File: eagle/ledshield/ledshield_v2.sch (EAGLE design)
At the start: 15 parts, among them U3 PCA9685

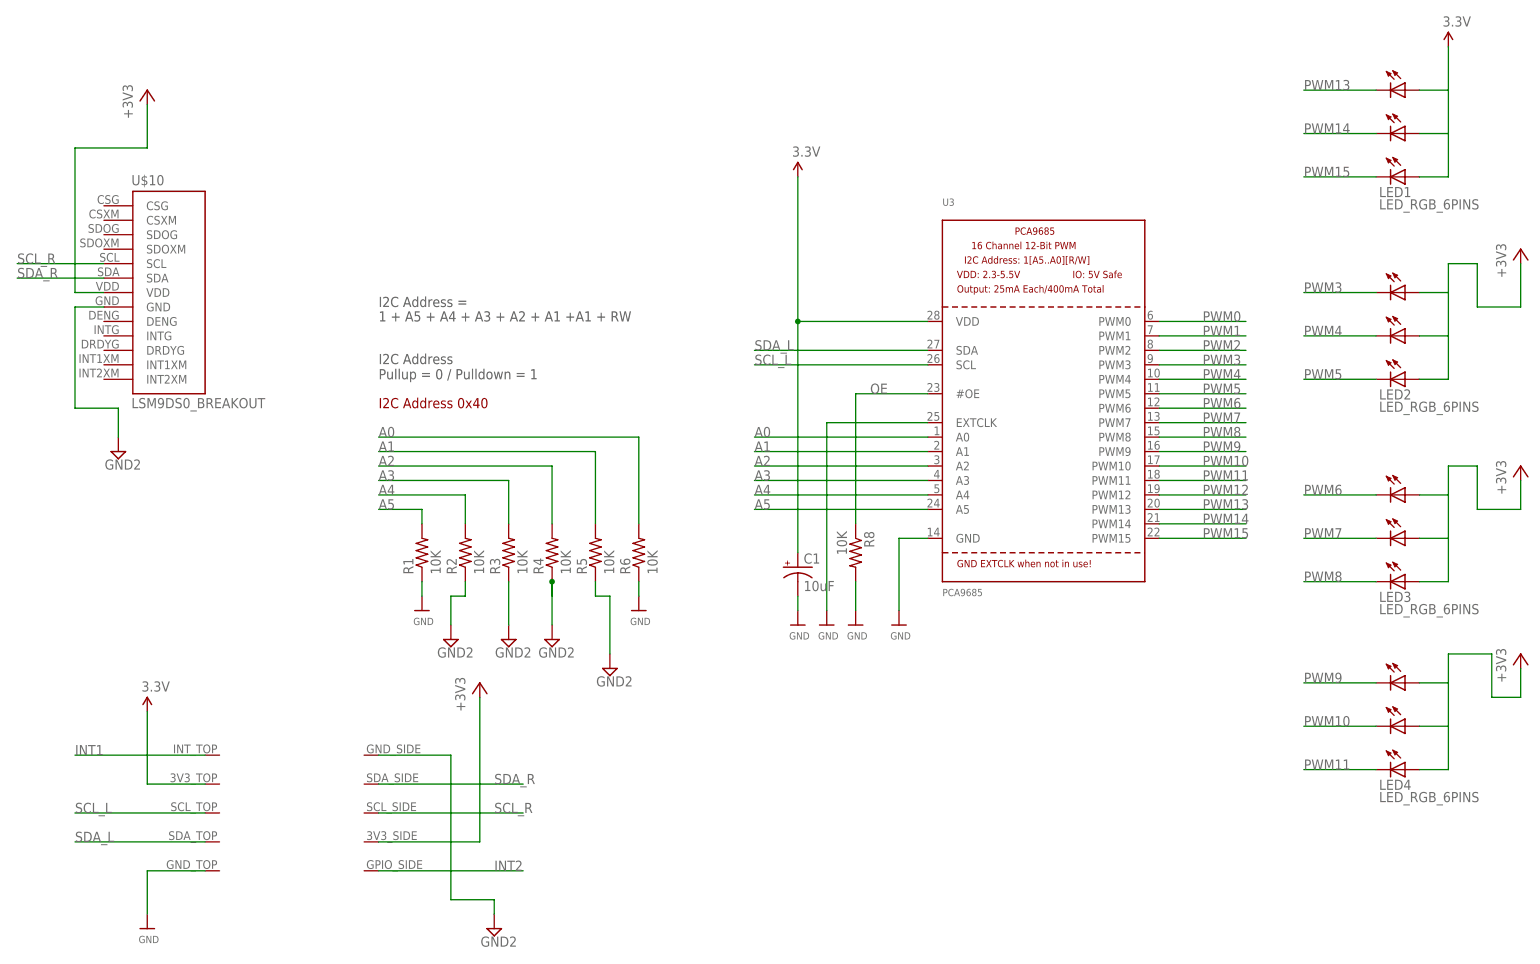
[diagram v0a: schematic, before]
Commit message: updated led shield design with common ground and passing design and electrical checks also started bluetooth/arduino communication to work in reverse from processing to arduino
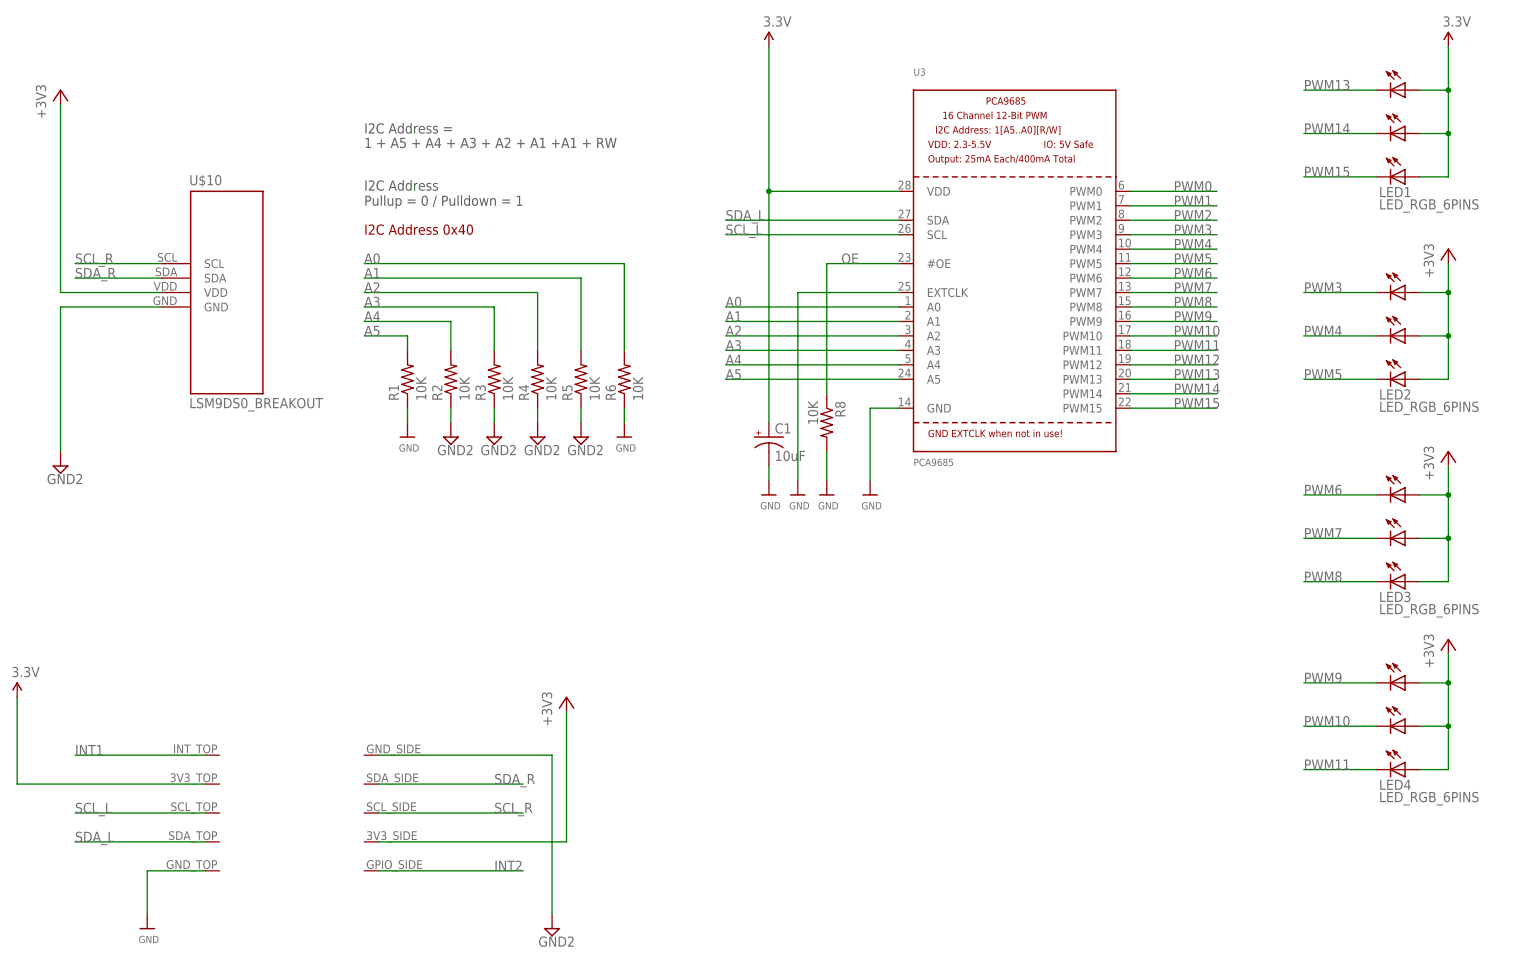
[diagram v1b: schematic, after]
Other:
- moved on the sheet: C1, R1, R2, R3, R4, R5, R6, R8, U3
